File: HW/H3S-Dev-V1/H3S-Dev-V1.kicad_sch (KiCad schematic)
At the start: 70 parts, among them J1 USB_C_Receptacle_USB2.0_16P, J2 Conn_01x02, J3 Conn_Coaxial, J4 Conn_01x04, J5 Conn_01x04, Q1 DMP3099L, SW1 SW_Push, SW2 SW_Push, U1 Ra-01SH-P, U2 LTC4054ES5-4.2, U3 USBLC6-2SC6, U4 ESP32-S3-WROOM-1, U5 SY8089AAAC, U6 L96-M33

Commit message: USB link updated
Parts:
- added R35, R36: 22, Resistor_SMD:R_0603_1608Metric, symbol Device:R
- added R37, R38: 1.5k, Resistor_SMD:R_0603_1608Metric, symbol Device:R
- R8: now not fitted
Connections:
- net RX: now also U4.37 (TXD0)
- net TX: now also U4.36 (RXD0)
- net VCC: now also R37.1, R38.1
- net at U3.4 (I/O2): now also R36.1, R37.2; no longer U4.14 (USB_D+)
- net at U3.6 (I/O1): now also R35.1, R38.2; no longer U4.13 (USB_D-)
- new net: R36.2, U4.14 (USB_D+)
- new net: R35.2, U4.13 (USB_D-)

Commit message: More progress today
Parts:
- C10, C11, J3, R18: now not fitted
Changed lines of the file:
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@@
 		(in_bom yes)
 		(on_board yes)
-		(dnp no)
+		(dnp yes)
 		(fields_autoplaced yes)
 		(property "Reference" "J3"
@@
 		(in_bom yes)
 		(on_board yes)
-		(dnp no)
+		(dnp yes)
 		(property "Reference" "R18"
 			(at 255.524 62.23 90)
@@
 		(in_bom yes)
 		(on_board yes)
-		(dnp no)
+		(dnp yes)
 		(property "Reference" "C11"
 			(at 257.048 68.58 0)
@@
 		(in_bom yes)
 		(on_board yes)
-		(dnp no)
+		(dnp yes)
 		(property "Reference" "C10"
 			(at 246.888 68.58 0)

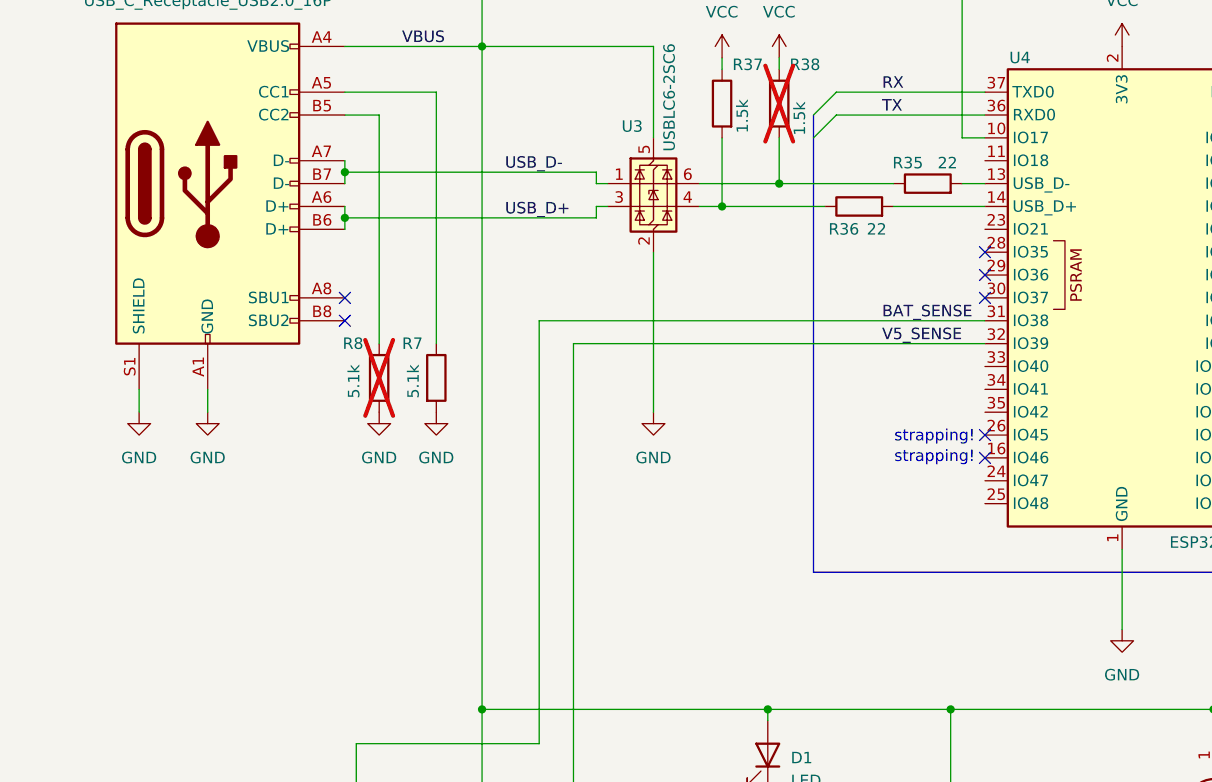
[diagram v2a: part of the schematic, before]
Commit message: USB Diff pair set up
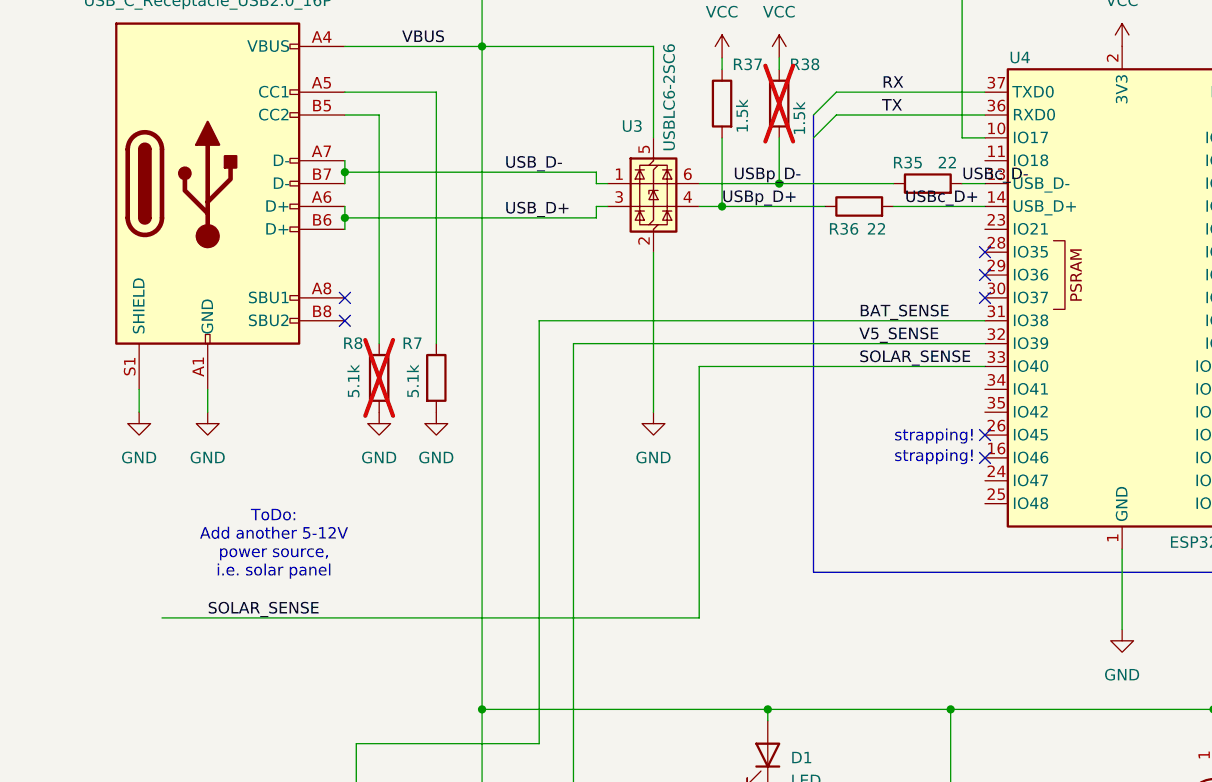
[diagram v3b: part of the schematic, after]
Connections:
- net USBp_D+: now reaches R36.1, R37.2, U3.4 (I/O2)
- net USBc_D+: now reaches R36.2, U4.14 (USB_D+)
- net USBp_D-: now reaches R35.1, R38.2, U3.6 (I/O1)
- net USBc_D-: now reaches R35.2, U4.13 (USB_D-)
- net SOLAR_SENSE: now reaches U4.33 (IO40)
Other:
- note added: "ToDo: Add another 5-12V power source, i.e. solar panel"
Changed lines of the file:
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@@
 		)
 	)
+	(text "ToDo:\nAdd another 5-12V\npower source,\ni.e. solar panel"
+		(exclude_from_sim no)
+		(at 50.546 167.132 0)
+		(effects
+			(font
+				(size 1.27 1.27)
+			)
+		)
+	)
 	(text "RESET"
 		(exclude_from_sim no)
@@
 	(wire
 		(pts
+			(xy 97.79 147.32) (xy 97.79 175.26)
+		)
+		(stroke
+			(width 0)
+			(type default)
+		)
+	)
+	(wire
+		(pts
 			(xy 219.71 139.7) (xy 219.71 142.24)
 		)
@@
 	(wire
 		(pts
+			(xy 38.1 175.26) (xy 97.79 175.26)
+		)
+		(stroke
+			(width 0)
+			(type default)
+		)
+	)
+	(wire
+		(pts
 			(xy 127 102.87) (xy 187.96 102.87)
 		)
@@
 	(wire
 		(pts
+			(xy 129.54 147.32) (xy 97.79 147.32)
+		)
+		(stroke
+			(width 0)
+			(type default)
+		)
+	)
+	(wire
+		(pts
 			(xy 279.4 119.38) (xy 284.48 119.38)
 		)
@@
 		)
 	)
+	(label "SOLAR_SENSE"
+		(at 43.18 175.26 0)
+		(effects
+			(font
+				(size 1.27 1.27)
+			)
+			(justify left bottom)
+		)
+	)
 	(label "LoRa_BUS"
 		(at 208.28 114.3 0)
@@
 		)
 	)
+	(label "USBp_D-"
+		(at 101.6 127 0)
+		(effects
+			(font
+				(size 1.27 1.27)
+			)
+			(justify left bottom)
+		)
+	)
 	(label "V5_SENSE"
 		(at 83.82 210.82 90)
@@
 	)
 	(label "V5_SENSE"
-		(at 118.11 144.78 0)
+		(at 115.57 144.78 0)
 		(effects
 			(font
@@
 	)
 	(label "BAT_SENSE"
-		(at 118.11 142.24 0)
+		(at 115.57 142.24 0)
 		(effects
 			(font
@@
 		)
 	)
+	(label "USBp_D+"
+		(at 100.33 129.54 0)
+		(effects
+			(font
+				(size 1.27 1.27)
+			)
+			(justify left bottom)
+		)
+	)
 	(label "SCL"
 		(at 275.59 109.22 180)
@@
 		)
 	)
+	(label "USBc_D-"
+		(at 127 127 0)
+		(effects
+			(font
+				(size 1.27 1.27)
+			)
+			(justify left bottom)
+		)
+	)
 	(label "DIO1"
 		(at 254 83.82 0)
@@
 		)
 	)
+	(label "SOLAR_SENSE"
+		(at 115.57 147.32 0)
+		(effects
+			(font
+				(size 1.27 1.27)
+			)
+			(justify left bottom)
+		)
+	)
 	(label "DIO1"
 		(at 163.83 162.56 0)
@@
 		(effects
 			(font
+				(size 1.27 1.27)
+			)
+			(justify left bottom)
+		)
+	)
+	(label "USBc_D+"
+		(at 120.65 129.54 0)
+		(effects
+			(font
